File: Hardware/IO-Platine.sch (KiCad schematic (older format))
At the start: 9 parts, among them J1 S8B-PH-SM4-TB, U4 TXB0104PWR

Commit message: Martin ist unförmig
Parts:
- removed S? (x2): GPTS203211B, digikey-footprints:PushButton_12x12mm_THT_GPTS203211B, symbol E-Ink:GPTS203211B
- added J502: Con.2-Pol, E-Ink:Pin-Header_1x2_2.54mm, symbol E-Ink:Con.2-Pol
- added Loch501, Loch502, Loch503, Loch504: Loch, symbol E-Ink:Loch
- added Logo501: Logo-OTH, symbol E-Ink:Logo-OTH
- added PS501: AAA_Batterypack, E-Ink:Pin-Header_1x2_2.54mm, symbol E-Ink:AAA_Batterypack
- added S501, S502: 1825910-6, digikey-footprints:Switch_Tactile_THT_6x6mm, symbol E-Ink:1825910-6
- gave numbers to parts that had none: 2
- renumbered C16 to C501, C17 to C502, J1 to J501, R8 to R501, U4 to U501
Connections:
- net labels added: +BATT, RX_D0, TX_D0
- wire segments 33 -> 36
- no-connect marks 0 -> 4
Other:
- note added: "3 * 1.5V AAA Battery -> 4,5V"
- note added: "UART-Interface for \n Programming\n"
- moved on the sheet: C501, C502, C503, C504, J501, R501, U501

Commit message: Ich hoffe wir koennen jetzt den Master mergen!
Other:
- note added: "kleinerer Kondensator + Pullup"
- note added: "kleinerer Kondensator + Pullup\n(5k 1n)"
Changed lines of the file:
@@
 NoConn ~ 9700 5550
 NoConn ~ 10100 5550
+Text Notes 8850 3950 0    20   ~ 4
+kleinerer Kondensator + Pullup
+Text Notes 9000 5450 0    20   ~ 4
+kleinerer Kondensator + Pullup\n(5k 1n)
 $EndSCHEMATC

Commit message: Zwischenspeicher Arbeit OTH
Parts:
- removed Loch501, Loch502, Loch503, Loch504: Loch, symbol E-Ink:Loch
- removed Logo501: Logo-OTH, symbol E-Ink:Logo-OTH
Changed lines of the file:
@@
 EESchema Schematic File Version 4
-EELAYER 30 0
+LIBS:E-Ink-cache
+EELAYER 29 0
 EELAYER END
 $Descr A4 11693 8268
@@
 	2300 2350 2100 2350
 $Comp
-L E-Ink:Logo-OTH Logo501
-U 1 1 5DEE1AF6
-P 2250 6100
-F 0 "Logo501" H 2328 6046 50  0000 L CNN
-F 1 "Logo-OTH" H 2328 5955 50  0000 L CNN
-F 2 "" H 2250 6100 50  0001 C CNN
-F 3 "" H 2250 6100 50  0001 C CNN
-	1    2250 6100
-	1    0    0    -1
-$EndComp
-$Comp
-L E-Ink:Loch Loch501
-U 1 1 5DEE1E1A
-P 2900 6100
-F 0 "Loch501" H 2978 6046 50  0000 L CNN
-F 1 "Loch" H 2978 5955 50  0000 L CNN
-F 2 "" H 2900 6100 50  0001 C CNN
-F 3 "" H 2900 6100 50  0001 C CNN
-	1    2900 6100
-	1    0    0    -1
-$EndComp
-$Comp
-L E-Ink:Loch Loch502
-U 1 1 5DEE22F1
-P 3300 6100
-F 0 "Loch502" H 3378 6046 50  0000 L CNN
-F 1 "Loch" H 3378 5955 50  0000 L CNN
-F 2 "" H 3300 6100 50  0001 C CNN
-F 3 "" H 3300 6100 50  0001 C CNN
-	1    3300 6100
-	1    0    0    -1
-$EndComp
-$Comp
-L E-Ink:Loch Loch503
-U 1 1 5DEE2E4E
-P 3700 6100
-F 0 "Loch503" H 3778 6046 50  0000 L CNN
-F 1 "Loch" H 3778 5955 50  0000 L CNN
-F 2 "" H 3700 6100 50  0001 C CNN
-F 3 "" H 3700 6100 50  0001 C CNN
-	1    3700 6100
-	1    0    0    -1
-$EndComp
-$Comp
-L E-Ink:Loch Loch504
-U 1 1 5DEE3804
-P 4100 6100
-F 0 "Loch504" H 4178 6046 50  0000 L CNN
-F 1 "Loch" H 4178 5955 50  0000 L CNN
-F 2 "" H 4100 6100 50  0001 C CNN
-F 3 "" H 4100 6100 50  0001 C CNN
-	1    4100 6100
-	1    0    0    -1
-$EndComp
-$Comp
 L E-Ink:Con.2-Pol J502

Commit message: save work at arges, finished layout and routing
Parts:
- J501: footprint (none) -> E-Ink:S8B-PH-SM4-TB
- S501, S502: footprint digikey-footprints:Switch_Tactile_THT_6x6mm -> Digikey:Switch_Tactile_SMD_6x6mm
- U501: footprint digikey-footprints:TSSOP-14_W4.4mm -> Digikey:TSSOP-14_W4.4mm
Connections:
- net CS: now also U501.2 (A1); no longer U501.5 (A4)
- net MISO: now also U501.5 (A4); no longer U501.2 (A1)
- net MOSI: now also U501.4 (A3); no longer U501.3 (A2)
- net SCK: now also U501.3 (A2); no longer U501.4 (A3)
- net at J501.3 (MISO): now also U501.10 (B4); no longer U501.13 (B1)
- net at J501.4 (MOSI): now also U501.11 (B3); no longer U501.12 (B2)
- net at J501.5 (SCK): now also U501.12 (B2); no longer U501.11 (B3)
- net at J501.6 (CS): now also U501.13 (B1); no longer U501.10 (B4)
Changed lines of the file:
@@
 EESchema Schematic File Version 4
 LIBS:E-Ink-cache
-EELAYER 29 0
+EELAYER 30 0
 EELAYER END
 $Descr A4 11693 8268
@@
 $EndDescr
 $Comp
-L E-Ink:S8B-PH-SM4-TB J?
-U 1 1 5DE794A9
-P 5950 3450
-AR Path="/5DE794A9" Ref="J?"  Part="1"
-AR Path="/5DE5A7F7/5DE794A9" Ref="J?"  Part="1"
-AR Path="/5DE7403E/5DE794A9" Ref="J501"  Part="1"
-F 0 "J501" H 6378 3151 50  0000 L CNN
-F 1 "S8B-PH-SM4-TB" H 6378 3060 50  0000 L CNN
-F 2 "" H 5900 3650 50  0001 C CNN
-F 3 "http://www.jst-mfg.com/product/pdf/eng/ePH.pdf" H 5900 3650 50  0001 C CNN
-F 4 "455-1755-1-ND" H 6300 3550 50  0001 C CNN "Digi-Key_PN"
-	1    5950 3450
-	1    0    0    -1
-$EndComp
-$Comp
-L power:GND #PWR?
-U 1 1 5DE794AF
-P 5950 3550
-AR Path="/5DE794AF" Ref="#PWR?"  Part="1"
-AR Path="/5DE5A7F7/5DE794AF" Ref="#PWR?"  Part="1"
-AR Path="/5DE7403E/5DE794AF" Ref="#PWR0511"  Part="1"
-F 0 "#PWR0511" H 5950 3300 50  0001 C CNN
-F 1 "GND" H 5955 3377 50  0000 C CNN
-F 2 "" H 5950 3550 50  0001 C CNN
-F 3 "" H 5950 3550 50  0001 C CNN
-	1    5950 3550
-	0    1    1    0
-$EndComp
-$Comp
-L power:+5V #PWR?
-U 1 1 5DE794B5
-P 5950 3450
-AR Path="/5DE794B5" Ref="#PWR?"  Part="1"
-AR Path="/5DE5A7F7/5DE794B5" Ref="#PWR?"  Part="1"
-AR Path="/5DE7403E/5DE794B5" Ref="#PWR0510"  Part="1"
-F 0 "#PWR0510" H 5950 3300 50  0001 C CNN
-F 1 "+5V" H 5965 3623 50  0000 C CNN
-F 2 "" H 5950 3450 50  0001 C CNN
-F 3 "" H 5950 3450 50  0001 C CNN
-	1    5950 3450
-	1    0    0    -1
-$EndComp
-$Comp
 L power:+5V #PWR?
 U 1 1 5DE794BB
@@
 	1    0    0    -1
 $EndComp
-Wire Wire Line
-	4000 3650 5950 3650
-Wire Wire Line
-	5950 3750 4000 3750
-Wire Wire Line
-	4000 3850 5950 3850
-Wire Wire Line
-	5950 3950 4000 3950
-Text GLabel 5950 4050 0    50   Input ~ 0
-RST_DIS
-Text GLabel 5950 4150 0    50   Output ~ 0
-BSY_DIS
 $Comp
 L E-Ink:TXB0104PWR U?
@@
 F 0 "U501" H 3234 3253 60  0000 C CNN
 F 1 "TXB0104PWR" H 3234 3147 60  0000 C CNN
-F 2 "digikey-footprints:TSSOP-14_W4.4mm" H 3900 4050 60  0001 L CNN
+F 2 "Digikey:TSSOP-14_W4.4mm" H 3900 4050 60  0001 L CNN
 F 3 "http://www.ti.com/general/docs/suppproductinfo.tsp?distId=10&gotoUrl=http%3A%2F%2Fwww.ti.com%2Flit%2Fgpn%2Ftxb0104" H 3900 4150 60  0001 L CNN
 F 4 "296-21929-1-ND" H 3900 4250 60  0001 L CNN "Digi-Key_PN"
@@
 $EndComp
 Wire Wire Line
+	2300 3950 3300 3950
+Wire Wire Line
+	2300 3850 3300 3850
+Wire Wire Line
+	2300 3750 3300 3750
+Wire Wire Line
 	2300 3650 3300 3650
-Wire Wire Line
-	2300 3750 3300 3750
-Wire Wire Line
-	2300 3850 3300 3850
-Wire Wire Line
-	2300 3950 3300 3950
 Wire Wire Line
 	2300 4050 3300 4050
 Text HLabel 2300 4050 0    50   Input ~ 10
 EN_SPI
+Text HLabel 2300 3650 0    50   Input ~ 10
+CS
+Text HLabel 2300 3750 0    50   Input ~ 10
+SCK
+Text HLabel 2300 3850 0    50   Input ~ 10
+MOSI
 Text HLabel 2300 3950 0    50   Input ~ 10
-CS
-Text HLabel 2300 3850 0    50   Input ~ 10
-SCK
-Text HLabel 2300 3750 0    50   Input ~ 10
-MOSI
-Text HLabel 2300 3650 0    50   Input ~ 10
 MISO
 Text HLabel 2300 4150 0    50   Output ~ 10
@@
 F 0 "S501" H 9900 3697 60  0000 C CNN
 F 1 "1825910-6" H 9900 3591 60  0000 C CNN
-F 2 "digikey-footprints:Switch_Tactile_THT_6x6mm" H 10100 3550 60  0001 L CNN
+F 2 "Digikey:Switch_Tactile_SMD_6x6mm" H 10100 3550 60  0001 L CNN
 F 3 "https://www.te.com/commerce/DocumentDelivery/DDEController?Action=srchrtrv&DocNm=1825910&DocType=Customer+Drawing&DocLang=English" H 10100 3650 60  0001 L CNN
 F 4 "450-1650-ND" H 10100 3750 60  0001 L CNN "Digi-Key_PN"
@@
 F 0 "S502" H 9900 5997 60  0000 C CNN
 F 1 "1825910-6" H 9900 5891 60  0000 C CNN
-F 2 "digikey-footprints:Switch_Tactile_THT_6x6mm" H 10100 5850 60  0001 L CNN
+F 2 "Digikey:Switch_Tactile_SMD_6x6mm" H 10100 5850 60  0001 L CNN
 F 3 "https://www.te.com/commerce/DocumentDelivery/DDEController?Action=srchrtrv&DocNm=1825910&DocType=Customer+Drawing&DocLang=English" H 10100 5950 60  0001 L CNN
 F 4 "450-1650-ND" H 10100 6050 60  0001 L CNN "Digi-Key_PN"
@@
 Text Notes 9000 5450 0    20   ~ 4
 kleinerer Kondensator + Pullup\n(5k 1n)
+Text GLabel 5950 3450 0    50   Output ~ 0
+BSY_DIS
+Text GLabel 5950 3550 0    50   Input ~ 0
+RST_DIS
+Wire Wire Line
+	5950 3650 4000 3650
+Wire Wire Line
+	4000 3750 5950 3750
+Wire Wire Line
+	5950 3850 4000 3850
+Wire Wire Line
+	4000 3950 5950 3950
+$Comp
+L power:+5V #PWR?
+U 1 1 5DE794B5
+P 5550 4200
+AR Path="/5DE794B5" Ref="#PWR?"  Part="1"
+AR Path="/5DE5A7F7/5DE794B5" Ref="#PWR?"  Part="1"
+AR Path="/5DE7403E/5DE794B5" Ref="#PWR0510"  Part="1"
+F 0 "#PWR0510" H 5550 4050 50  0001 C CNN
+F 1 "+5V" H 5565 4373 50  0000 C CNN
+F 2 "" H 5550 4200 50  0001 C CNN
+F 3 "" H 5550 4200 50  0001 C CNN
+	1    5550 4200
+	-1   0    0    -1
+$EndComp
+$Comp
+L power:GND #PWR?
+U 1 1 5DE794AF
+P 5950 4050
+AR Path="/5DE794AF" Ref="#PWR?"  Part="1"
+AR Path="/5DE5A7F7/5DE794AF" Ref="#PWR?"  Part="1"
+AR Path="/5DE7403E/5DE794AF" Ref="#PWR0511"  Part="1"
+F 0 "#PWR0511" H 5950 3800 50  0001 C CNN
+F 1 "GND" H 5955 3877 50  0000 C CNN
+F 2 "" H 5950 4050 50  0001 C CNN
+F 3 "" H 5950 4050 50  0001 C CNN
+	1    5950 4050
+	0    1    -1   0
+$EndComp
+$Comp
+L E-Ink:S8B-PH-SM4-TB J?
+U 1 1 5DE794A9
+P 5950 4150
+AR Path="/5DE794A9" Ref="J?"  Part="1"
+AR Path="/5DE5A7F7/5DE794A9" Ref="J?"  Part="1"
+AR Path="/5DE7403E/5DE794A9" Ref="J501"  Part="1"
+F 0 "J501" H 6378 3851 50  0000 L CNN
+F 1 "S8B-PH-SM4-TB" H 6378 3760 50  0000 L CNN
+F 2 "E-Ink:S8B-PH-SM4-TB" H 5900 4350 50  0001 C CNN
+F 3 "http://www.jst-mfg.com/product/pdf/eng/ePH.pdf" H 5900 4350 50  0001 C CNN
+F 4 "455-1755-1-ND" H 6300 4250 50  0001 C CNN "Digi-Key_PN"
+	1    5950 4150
+	1    0    0    1
+$EndComp
+Wire Wire Line
+	5550 4200 5950 4200
+Wire Wire Line
+	5950 4200 5950 4150
 $EndSCHEMATC

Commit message: savecommit
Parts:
- R501: value 47k -> 4k7; symbol E-Ink:47k -> E-Ink:4k7
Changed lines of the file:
@@
 EESchema Schematic File Version 4
-LIBS:E-Ink-cache
 EELAYER 30 0
 EELAYER END
@@
 $EndComp
 $Comp
-L E-Ink:47k R?
+L E-Ink:4k7 R?
 U 1 1 5DE22A83
 P 9000 5450
@@
 AR Path="/5DE7403E/5DE22A83" Ref="R501"  Part="1"
 F 0 "R501" V 9054 5478 50  0000 L CNN
-F 1 "47k" V 9145 5478 50  0000 L CNN
+F 1 "4k7" V 9145 5478 50  0000 L CNN
 F 2 "Resistor_SMD:R_0805_2012Metric_Pad1.15x1.40mm_HandSolder" H 9050 5300 50  0001 C CNN
 F 3 "" H 9000 5500 50  0001 C CNN

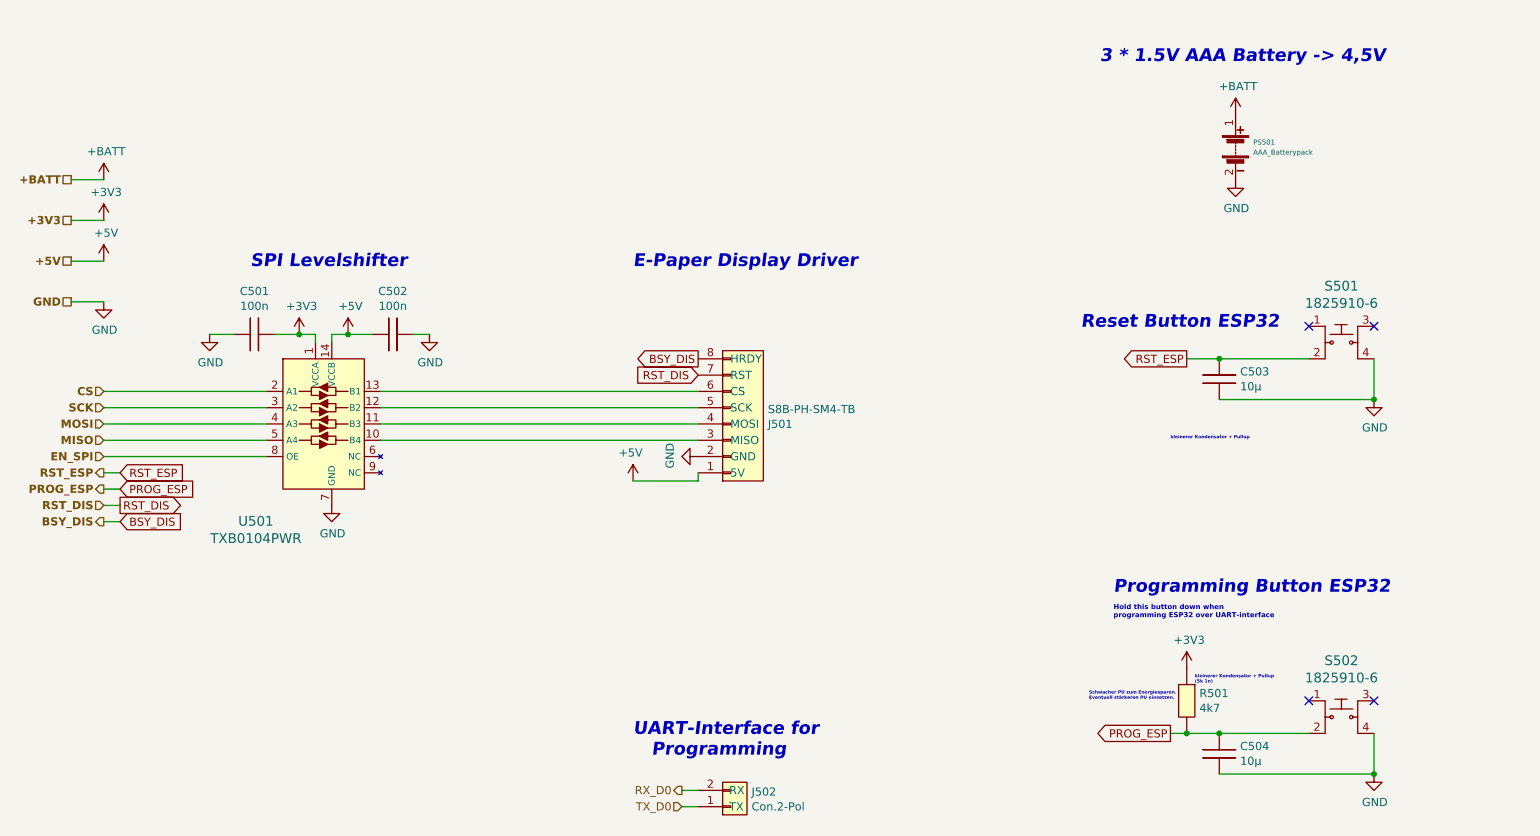
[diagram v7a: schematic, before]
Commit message: Added new MCU and redesigned schematics
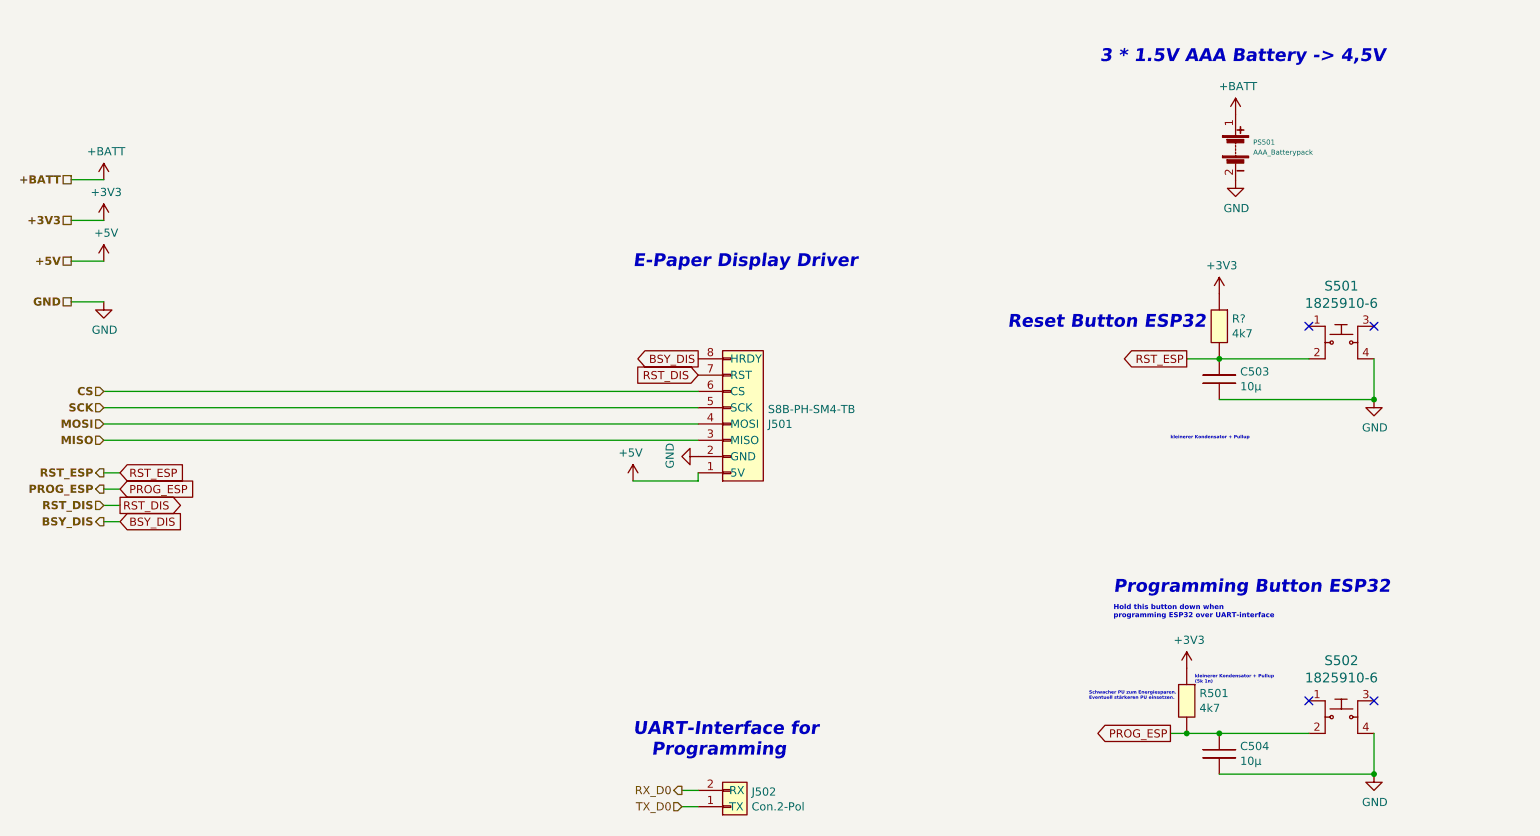
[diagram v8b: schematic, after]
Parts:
- removed C501, C502: 100n, Capacitor_SMD:C_0805_2012Metric_Pad1.15x1.40mm_HandSolder, symbol E-Ink:100n
- removed U501: TXB0104PWR, Digikey:TSSOP-14_W4.4mm, symbol E-Ink:TXB0104PWR
- added R?: 4k7, Resistor_SMD:R_0805_2012Metric_Pad1.15x1.40mm_HandSolder, symbol E-Ink:4k7
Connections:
- net +3V3: now also R?.1
- net CS: now also J501.6 (CS)
- net MISO: now also J501.3 (MISO)
- net MOSI: now also J501.4 (MOSI)
- net RST_ESP: now also R?.2
- net SCK: now also J501.5 (SCK)
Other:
- note removed: "SPI Levelshifter \n"
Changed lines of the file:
@@
 EESchema Schematic File Version 4
-LIBS:E-Ink-cache
 EELAYER 30 0
 EELAYER END
@@
 Comment4 ""
 $EndDescr
-$Comp
-L power:+5V #PWR?
-U 1 1 5DE794BB
-P 3800 3300
-AR Path="/5DE794BB" Ref="#PWR?"  Part="1"
-AR Path="/5DE5A7F7/5DE794BB" Ref="#PWR?"  Part="1"
-AR Path="/5DE7403E/5DE794BB" Ref="#PWR0508"  Part="1"
-F 0 "#PWR0508" H 3800 3150 50  0001 C CNN
-F 1 "+5V" H 3815 3473 50  0000 C CNN
-F 2 "" H 3800 3300 50  0001 C CNN
-F 3 "" H 3800 3300 50  0001 C CNN
-	1    3800 3300
-	1    0    0    -1
-$EndComp
-$Comp
-L power:+3V3 #PWR?
-U 1 1 5DE794C1
-P 3500 3300
-AR Path="/5DE794C1" Ref="#PWR?"  Part="1"
-AR Path="/5DE5A7F7/5DE794C1" Ref="#PWR?"  Part="1"
-AR Path="/5DE7403E/5DE794C1" Ref="#PWR0506"  Part="1"
-F 0 "#PWR0506" H 3500 3150 50  0001 C CNN
-F 1 "+3V3" H 3515 3473 50  0000 C CNN
-F 2 "" H 3500 3300 50  0001 C CNN
-F 3 "" H 3500 3300 50  0001 C CNN
-	1    3500 3300
-	1    0    0    -1
-$EndComp
-Wire Wire Line
-	3500 3300 3600 3300
-Wire Wire Line
-	3600 3300 3600 3350
-Wire Wire Line
-	3700 3350 3700 3300
-Wire Wire Line
-	3700 3300 3800 3300
-$Comp
-L power:GND #PWR?
-U 1 1 5DE794CB
-P 3700 4350
-AR Path="/5DE794CB" Ref="#PWR?"  Part="1"
-AR Path="/5DE5A7F7/5DE794CB" Ref="#PWR?"  Part="1"
-AR Path="/5DE7403E/5DE794CB" Ref="#PWR0507"  Part="1"
-F 0 "#PWR0507" H 3700 4100 50  0001 C CNN
-F 1 "GND" H 3705 4177 50  0000 C CNN
-F 2 "" H 3700 4350 50  0001 C CNN
-F 3 "" H 3700 4350 50  0001 C CNN
-	1    3700 4350
-	1    0    0    -1
-$EndComp
-$Comp
-L E-Ink:TXB0104PWR U?
-U 1 1 5DE794E5
-P 3700 3850
-AR Path="/5DE794E5" Ref="U?"  Part="1"
-AR Path="/5DE5A7F7/5DE794E5" Ref="U?"  Part="1"
-AR Path="/5DE7403E/5DE794E5" Ref="U501"  Part="1"
-F 0 "U501" H 3234 3253 60  0000 C CNN
-F 1 "TXB0104PWR" H 3234 3147 60  0000 C CNN
-F 2 "Digikey:TSSOP-14_W4.4mm" H 3900 4050 60  0001 L CNN
-F 3 "http://www.ti.com/general/docs/suppproductinfo.tsp?distId=10&gotoUrl=http%3A%2F%2Fwww.ti.com%2Flit%2Fgpn%2Ftxb0104" H 3900 4150 60  0001 L CNN
-F 4 "296-21929-1-ND" H 3900 4250 60  0001 L CNN "Digi-Key_PN"
-F 5 "TXB0104PWR" H 3900 4350 60  0001 L CNN "MPN"
-F 6 "Integrated Circuits (ICs)" H 3900 4450 60  0001 L CNN "Category"
-F 7 "Logic - Translators, Level Shifters" H 3900 4550 60  0001 L CNN "Family"
-F 8 "http://www.ti.com/general/docs/suppproductinfo.tsp?distId=10&gotoUrl=http%3A%2F%2Fwww.ti.com%2Flit%2Fgpn%2Ftxb0104" H 3900 4650 60  0001 L CNN "DK_Datasheet_Link"
-F 9 "/product-detail/en/texas-instruments/TXB0104PWR/296-21929-1-ND/1629282" H 3900 4750 60  0001 L CNN "DK_Detail_Page"
-F 10 "IC TRNSLTR BIDIRECTIONAL 14TSSOP" H 3900 4850 60  0001 L CNN "Description"
-F 11 "Texas Instruments" H 3900 4950 60  0001 L CNN "Manufacturer"
-F 12 "Active" H 3900 5050 60  0001 L CNN "Status"
-	1    3700 3850
-	1    0    0    -1
-$EndComp
-Text Notes 3200 2900 0    79   Italic 16
-SPI Levelshifter \n
-$Comp
-L E-Ink:100n C?
-U 1 1 5DE794EC
-P 3250 3150
-AR Path="/5DE794EC" Ref="C?"  Part="1"
-AR Path="/5DE5A7F7/5DE794EC" Ref="C?"  Part="1"
-AR Path="/5DE7403E/5DE794EC" Ref="C501"  Part="1"
-F 0 "C501" H 3225 3265 50  0000 C CNN
-F 1 "100n" H 3225 3174 50  0000 C CNN
-F 2 "Capacitor_SMD:C_0805_2012Metric_Pad1.15x1.40mm_HandSolder" H 3250 2850 50  0001 C CNN
-F 3 "" H 3200 3150 50  0001 C CNN
-	1    3250 3150
-	1    0    0    -1
-$EndComp
-$Comp
-L E-Ink:100n C?
-U 1 1 5DE794F2
-P 4100 3150
-AR Path="/5DE794F2" Ref="C?"  Part="1"
-AR Path="/5DE5A7F7/5DE794F2" Ref="C?"  Part="1"
-AR Path="/5DE7403E/5DE794F2" Ref="C502"  Part="1"
-F 0 "C502" H 4075 3265 50  0000 C CNN
-F 1 "100n" H 4075 3174 50  0000 C CNN
-F 2 "Capacitor_SMD:C_0805_2012Metric_Pad1.15x1.40mm_HandSolder" H 4100 2850 50  0001 C CNN
-F 3 "" H 4050 3150 50  0001 C CNN
-	1    4100 3150
-	1    0    0    -1
-$EndComp
-$Comp
-L power:GND #PWR?
-U 1 1 5DE794F8
-P 2950 3300
-AR Path="/5DE794F8" Ref="#PWR?"  Part="1"
-AR Path="/5DE5A7F7/5DE794F8" Ref="#PWR?"  Part="1"
-AR Path="/5DE7403E/5DE794F8" Ref="#PWR0505"  Part="1"
-F 0 "#PWR0505" H 2950 3050 50  0001 C CNN
-F 1 "GND" H 2955 3127 50  0000 C CNN
-F 2 "" H 2950 3300 50  0001 C CNN
-F 3 "" H 2950 3300 50  0001 C CNN
-	1    2950 3300
-	1    0    0    -1
-$EndComp
-$Comp
-L power:GND #PWR?
-U 1 1 5DE794FE
-P 4300 3300
-AR Path="/5DE794FE" Ref="#PWR?"  Part="1"
-AR Path="/5DE5A7F7/5DE794FE" Ref="#PWR?"  Part="1"
-AR Path="/5DE7403E/5DE794FE" Ref="#PWR0509"  Part="1"
-F 0 "#PWR0509" H 4300 3050 50  0001 C CNN
-F 1 "GND" H 4305 3127 50  0000 C CNN
-F 2 "" H 4300 3300 50  0001 C CNN
-F 3 "" H 4300 3300 50  0001 C CNN
-	1    4300 3300
-	1    0    0    -1
-$EndComp
-Wire Wire Line
-	4200 3300 4300 3300
-Wire Wire Line
-	3950 3300 3800 3300
-Connection ~ 3800 3300
-Wire Wire Line
-	3500 3300 3350 3300
-Connection ~ 3500 3300
-Wire Wire Line
-	3100 3300 2950 3300
 Text GLabel 8950 3450 0    50   Output ~ 0
 RST_ESP
@@
 	1    0    0    -1
 $EndComp
-Wire Wire Line
-	2300 3950 3300 3950
-Wire Wire Line
-	2300 3850 3300 3850
-Wire Wire Line
-	2300 3750 3300 3750
-Wire Wire Line
-	2300 3650 3300 3650
-Wire Wire Line
-	2300 4050 3300 4050
-Text HLabel 2300 4050 0    50   Input ~ 10
-EN_SPI
 Text HLabel 2300 3650 0    50   Input ~ 10
 CS
@@
 Wire Wire Line
 	2400 4450 2300 4450
-Text Notes 8300 3400 0    79   Italic 16
+Text Notes 7850 3400 0    79   Italic 16
 Reset Button ESP32\n\n
 Text GLabel 8850 5750 0    50   Output ~ 0
@@
 Text GLabel 5950 3550 0    50   Input ~ 0
 RST_DIS
-Wire Wire Line
-	5950 3650 4000 3650
-Wire Wire Line
-	4000 3750 5950 3750
-Wire Wire Line
-	5950 3850 4000 3850
-Wire Wire Line
-	4000 3950 5950 3950
 $Comp
 L power:+5V #PWR?
@@
 Wire Wire Line
 	5950 4200 5950 4150
+Wire Wire Line
+	2300 3650 5950 3650
+Wire Wire Line
+	2300 3750 5950 3750
+Wire Wire Line
+	2300 3850 5950 3850
+Wire Wire Line
+	2300 3950 5950 3950
+$Comp
+L power:+3V3 #PWR?
+U 1 1 5F894235
+P 9150 3050
+AR Path="/5F894235" Ref="#PWR?"  Part="1"
+AR Path="/5DE5A7F7/5F894235" Ref="#PWR?"  Part="1"
+AR Path="/5DE7403E/5F894235" Ref="#PWR?"  Part="1"
+F 0 "#PWR?" H 9150 2900 50  0001 C CNN
+F 1 "+3V3" H 9165 3223 50  0000 C CNN
+F 2 "" H 9150 3050 50  0001 C CNN
+F 3 "" H 9150 3050 50  0001 C CNN
+	1    9150 3050
+	1    0    0    -1
+$EndComp
+$Comp
+L E-Ink:4k7 R?
+U 1 1 5F89423B
+P 9200 3150
+AR Path="/5F89423B" Ref="R?"  Part="1"
+AR Path="/5DE4BC0A/5F89423B" Ref="R?"  Part="1"
+AR Path="/5DE7403E/5F89423B" Ref="R?"  Part="1"
+F 0 "R?" V 9254 3178 50  0000 L CNN
+F 1 "4k7" V 9345 3178 50  0000 L CNN
+F 2 "Resistor_SMD:R_0805_2012Metric_Pad1.15x1.40mm_HandSolder" H 9250 3000 50  0001 C CNN
+F 3 "" H 9200 3200 50  0001 C CNN
+	1    9200 3150
+	0    1    1    0
+$EndComp
 $EndSCHEMATC
